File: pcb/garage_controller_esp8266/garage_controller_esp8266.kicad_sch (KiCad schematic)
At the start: 38 parts, among them J1 Connections, J2 Conn_01x03_Socket, Q1 2N7002, Q2 2N7002, Q3 2N7002, U1 Wemos D1 mini connector, U2 MCP23017_SO

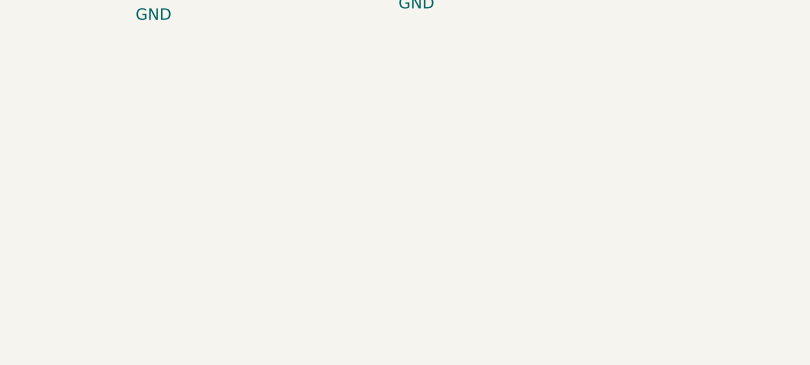
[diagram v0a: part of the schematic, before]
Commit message: Changed pins for buttons and added clipper
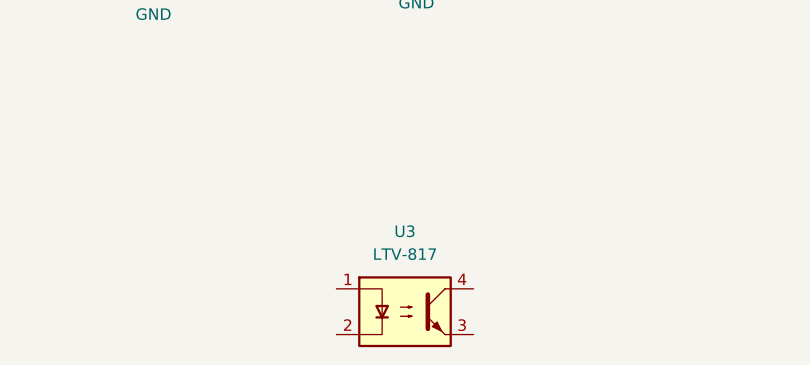
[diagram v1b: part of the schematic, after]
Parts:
- added U3: LTV-817, Package_DIP:DIP-4_W7.62mm, symbol Isolator:LTV-817
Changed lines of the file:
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@@
+	)
+	(symbol
+		(lib_id "Isolator:LTV-817")
+		(at 83.82 146.05 0)
+		(unit 1)
+		(exclude_from_sim no)
+		(in_bom yes)
+		(on_board yes)
+		(dnp no)
+		(fields_autoplaced yes)
+		(property "Reference" "U3"
+			(at 83.82 137.16 0)
+			(effects
+				(font
+					(size 1.27 1.27)
+				)
+			)
+		)
+		(property "Value" "LTV-817"
+			(at 83.82 139.7 0)
+			(effects
+				(font
+					(size 1.27 1.27)
+				)
+			)
+		)
+		(property "Footprint" "Package_DIP:DIP-4_W7.62mm"
+			(at 78.74 151.13 0)
+			(effects
+				(font
+					(size 1.27 1.27)
+					(italic yes)
+				)
+				(justify left)
+				(hide yes)
+			)
+		)
+		(property "Datasheet" "http://www.us.liteon.com/downloads/LTV-817-827-847.PDF"
+			(at 83.82 148.59 0)
+			(effects
+				(font
+					(size 1.27 1.27)
+				)
+				(justify left)
+				(hide yes)
+			)
+		)
+		(property "Description" "DC Optocoupler, Vce 35V, CTR 50%, DIP-4"
+			(at 83.82 146.05 0)
+			(effects
+				(font
+					(size 1.27 1.27)
+				)
+				(hide yes)
+			)
+		)
+		(pin "2"
+		)
+		(pin "1"
+		)
+		(pin "4"
+		)
+		(pin "3"
+		)
+		(instances
+			(project ""
+				(path "/a3368ded-dbda-4598-8dff-6b66bf86fe1a"
+					(reference "U3")
+					(unit 1)
+				)
+			)
+		)
 	)
 	(symbol
